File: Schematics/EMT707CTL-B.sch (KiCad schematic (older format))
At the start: 47 parts, among them CON1 CONN_01X09, P1 CONN_01X02, U1 ADE7753

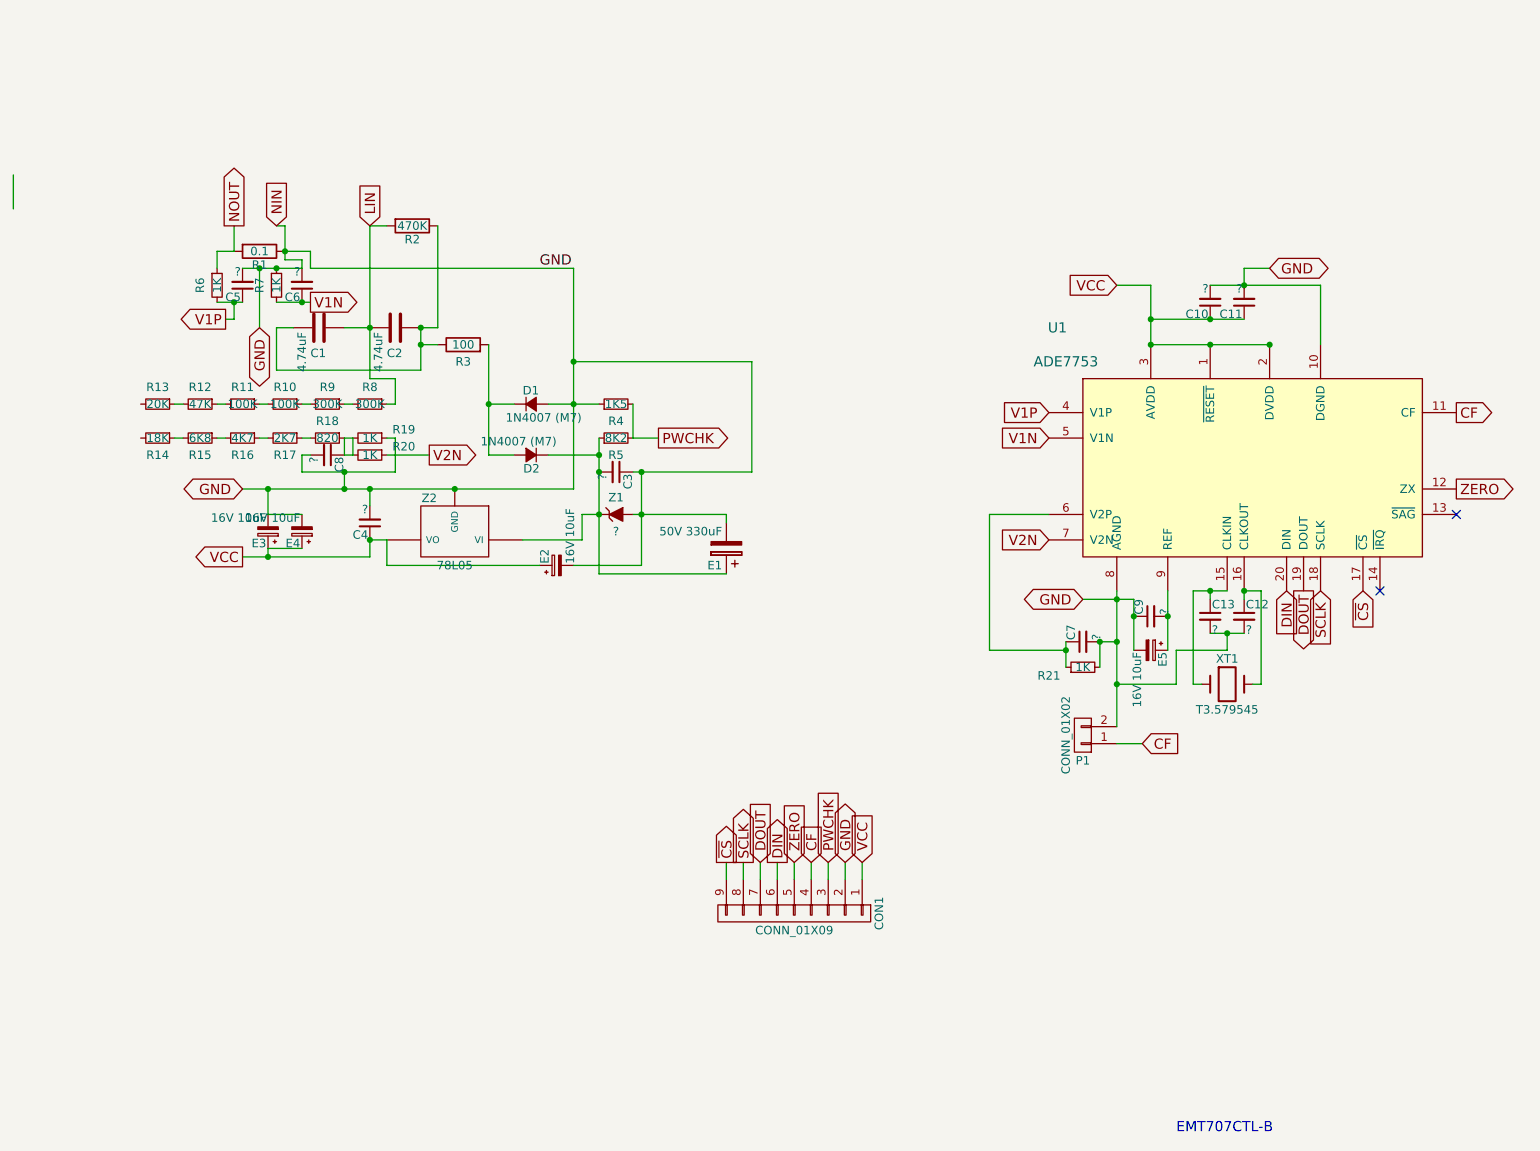
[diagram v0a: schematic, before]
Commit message: Fix some nets and errors, use svg export instead of pdf
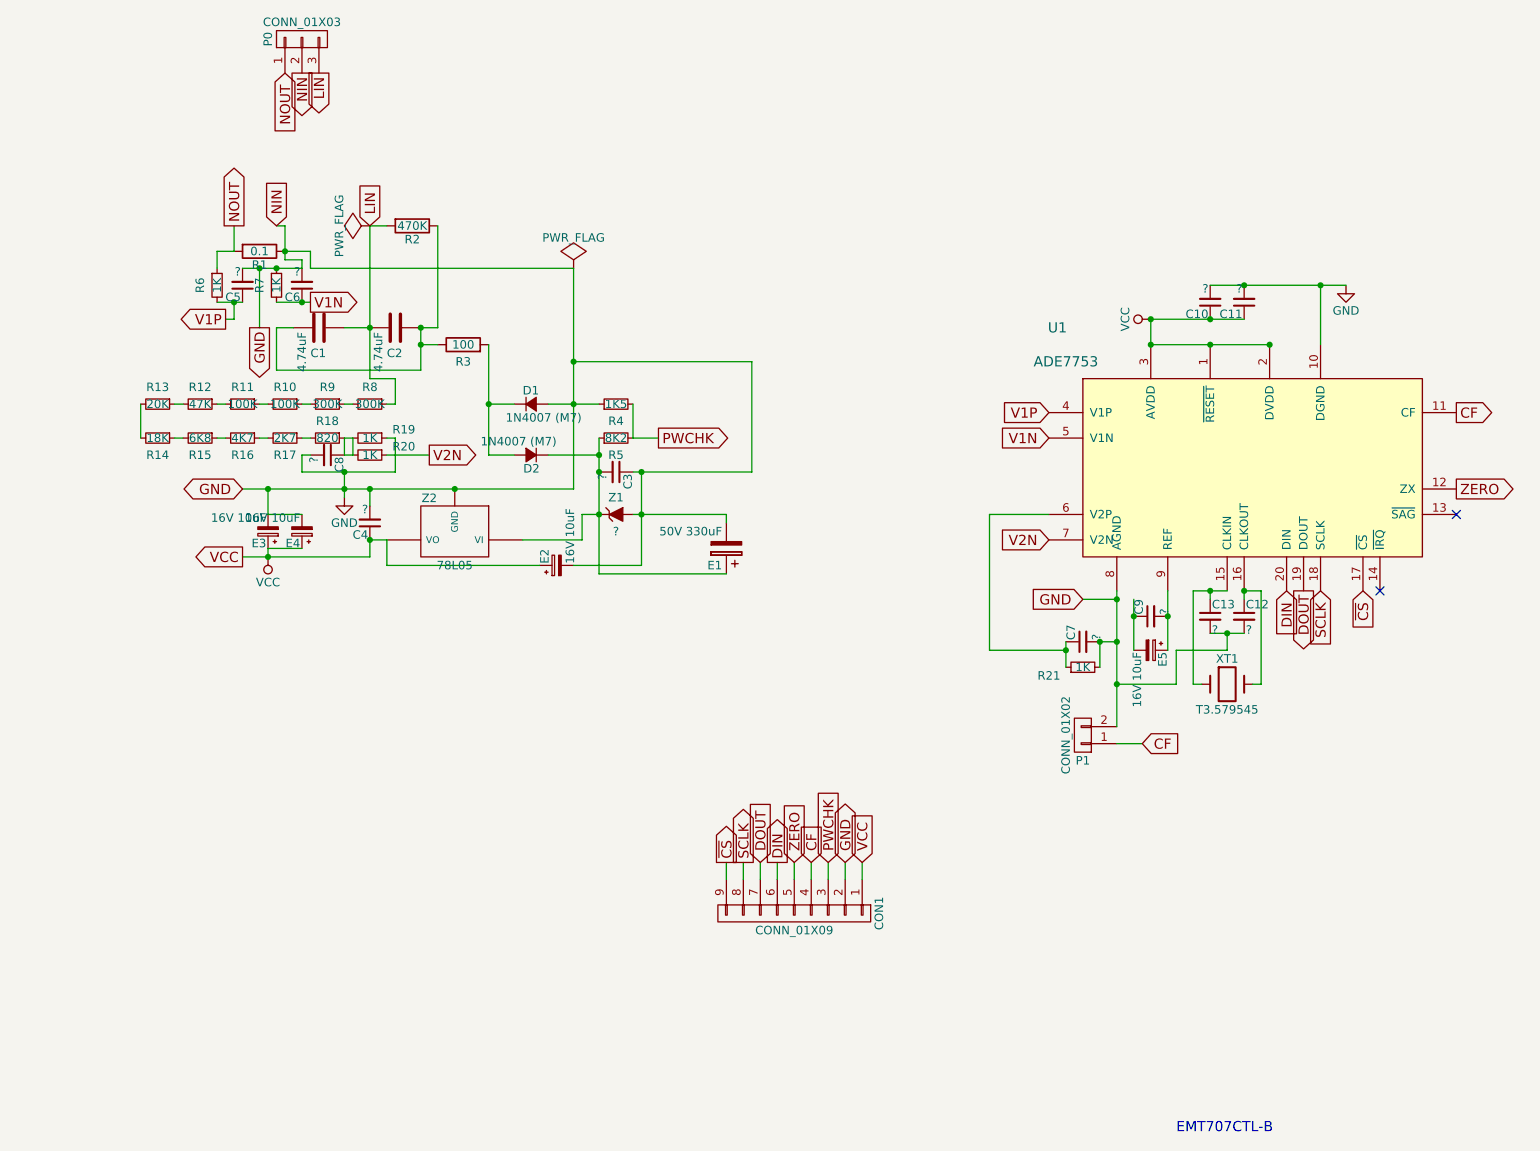
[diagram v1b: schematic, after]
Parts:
- added P0: CONN_01X03, symbol CONN_01X03
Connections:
- net GND: now also P0.2 (P2); no longer C9.1, E5.2
- net LIN: now also P0.3 (P3)
- net NOUT: now also P0.1 (P1)
- net at R13.2: now also R14.2
- new net: C9.1, E5.2
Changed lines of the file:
@@
 LIBS:contrib
 LIBS:valves
+LIBS:ade7753
 EELAYER 25 0
 EELAYER END
@@
 Text GLabel 2150 2150 1    60   Input ~ 0
 NIN
-Text GLabel 2700 2150 1    60   Input ~ 0
-LIN
 $Comp
 L R R2
@@
 	0    1    1    0
 $EndComp
-Text Label 3700 2400 0    60   ~ 0
-GND
 $Comp
 L CP E1
@@
 Text GLabel 6700 3400 0    60   Input ~ 0
 V1N
-Text GLabel 2050 2750 3    60   BiDi ~ 0
+Text GLabel 2050 2750 3    60   Output ~ 0
 GND
 Text GLabel 1850 2700 0    60   Output ~ 0
@@
 	0    -1   -1   0
 $EndComp
-Text GLabel 6900 4350 0    60   BiDi ~ 0
+Text GLabel 6900 4350 0    60   Input ~ 0
 GND
 $Comp
@@
 	-1   0    0    1
 $EndComp
-Text GLabel 7100 2500 0    60   Input ~ 0
-VCC
-Text GLabel 8000 2400 2    60   BiDi ~ 0
-GND
 $Comp
 L Crystal XT1
@@
 	2550 3400 2600 3400
 Wire Wire Line
-	600  2050 600  1850
-Wire Wire Line
 	2550 3400 2550 3500
 Wire Wire Line
@@
 	2300 3500 2350 3500
 Wire Wire Line
-	2550 3600 2550 3700
+	2550 3600 2550 3750
 Connection ~ 2550 3700
 Connection ~ 2550 3600
-Wire Wire Line
-	7100 2500 7300 2500
-Wire Wire Line
-	7300 2500 7300 2850
 Connection ~ 7650 2850
 Connection ~ 7300 2850
 Connection ~ 8000 2850
 Wire Wire Line
-	6900 4350 7200 4350
-Wire Wire Line
-	7100 4300 7100 5100
-Wire Wire Line
 	7400 4300 7400 4650
 Connection ~ 7400 4450
 Wire Wire Line
 	7200 4350 7200 4650
-Connection ~ 7100 4350
 Connection ~ 7200 4450
 Wire Wire Line
@@
 	7300 2850 8000 2850
 Wire Wire Line
-	8000 2400 7850 2400
-Wire Wire Line
-	7850 2400 7850 2500
-Wire Wire Line
-	7650 2500 8300 2500
+	7650 2500 8450 2500
 Connection ~ 7850 2500
 Wire Wire Line
@@
 Text Notes 7450 7500 0    60   ~ 0
 EMT707CTL-B
+Wire Wire Line
+	1350 3200 1350 3400
+Wire Wire Line
+	7100 4300 7100 5100
+Wire Wire Line
+	6900 4350 7100 4350
+Connection ~ 7100 4350
+$Comp
+L GND #PWR01
+U 1 1 59159E6F
+P 2550 3750
+F 0 "#PWR01" H 2550 3500 50  0001 C CNN
+F 1 "GND" H 2550 3600 50  0000 C CNN
+F 2 "" H 2550 3750 50  0000 C CNN
+F 3 "" H 2550 3750 50  0000 C CNN
+	1    2550 3750
+	1    0    0    -1
+$EndComp
+$Comp
+L VCC #PWR02
+U 1 1 59159F10
+P 2100 4100
+F 0 "#PWR02" H 2100 3950 50  0001 C CNN
+F 1 "VCC" H 2100 4250 50  0000 C CNN
+F 2 "" H 2100 4100 50  0000 C CNN
+F 3 "" H 2100 4100 50  0000 C CNN
+	1    2100 4100
+	-1   0    0    1
+$EndComp
+$Comp
+L VCC #PWR03
+U 1 1 5915AF4A
+P 7300 2700
+F 0 "#PWR03" H 7300 2550 50  0001 C CNN
+F 1 "VCC" H 7300 2850 50  0000 C CNN
+F 2 "" H 7300 2700 50  0000 C CNN
+F 3 "" H 7300 2700 50  0000 C CNN
+	1    7300 2700
+	0    -1   -1   0
+$EndComp
+Wire Wire Line
+	7300 2700 7300 2850
+$Comp
+L GND #PWR04
+U 1 1 5915B117
+P 8450 2500
+F 0 "#PWR04" H 8450 2250 50  0001 C CNN
+F 1 "GND" H 8450 2350 50  0000 C CNN
+F 2 "" H 8450 2500 50  0000 C CNN
+F 3 "" H 8450 2500 50  0000 C CNN
+	1    8450 2500
+	1    0    0    -1
+$EndComp
+Connection ~ 8300 2500
+Text GLabel 2700 2150 1    60   Input ~ 0
+LIN
+Text GLabel 2400 1250 3    60   Output ~ 0
+LIN
+Text GLabel 2200 1250 3    60   Input ~ 0
+NOUT
+Text GLabel 2300 1250 3    60   Output ~ 0
+NIN
+$Comp
+L CONN_01X03 P0
+U 1 1 5915C428
+P 2300 1050
+F 0 "P0" H 2300 1250 50  0000 C CNN
+F 1 "CONN_01X03" V 2400 1050 50  0000 C CNN
+F 2 "" H 2300 1050 50  0000 C CNN
+F 3 "" H 2300 1050 50  0000 C CNN
+	1    2300 1050
+	0    -1   -1   0
+$EndComp
+$Comp
+L PWR_FLAG #FLG05
+U 1 1 59161A0C
+P 3900 2400
+F 0 "#FLG05" H 3900 2495 50  0001 C CNN
+F 1 "PWR_FLAG" H 3900 2580 50  0000 C CNN
+F 2 "" H 3900 2400 50  0000 C CNN
+F 3 "" H 3900 2400 50  0000 C CNN
+	1    3900 2400
+	1    0    0    -1
+$EndComp
+$Comp
+L PWR_FLAG #FLG06
+U 1 1 59161B0E
+P 2700 2150
+F 0 "#FLG06" H 2700 2245 50  0001 C CNN
+F 1 "PWR_FLAG" H 2700 2330 50  0000 C CNN
+F 2 "" H 2700 2150 50  0000 C CNN
+F 3 "" H 2700 2150 50  0000 C CNN
+	1    2700 2150
+	0    -1   -1   0
+$EndComp
 $EndSCHEMATC
